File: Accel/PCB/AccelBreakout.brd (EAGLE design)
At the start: 15.2 x 12.7 mm, 10 parts

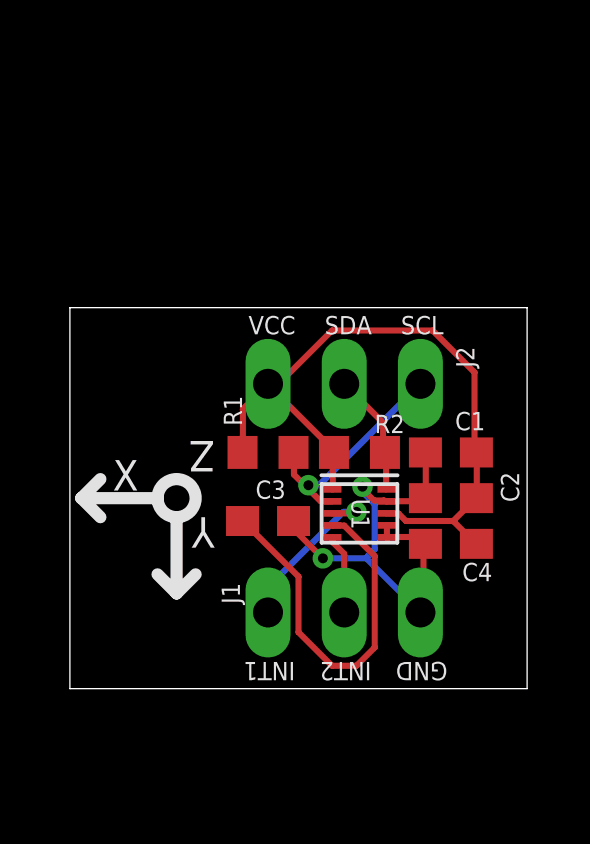
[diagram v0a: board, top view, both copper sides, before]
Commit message: accel - size, layout, labels
Adjusted size to be 0.6" DIP spacing.  Better orientation and position of all
labels.  Completely rerouted to remove all vias.
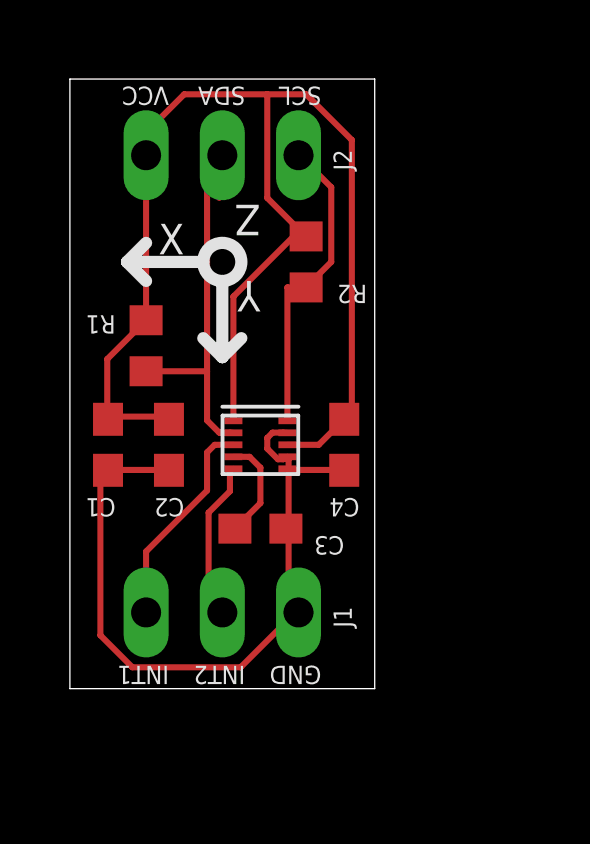
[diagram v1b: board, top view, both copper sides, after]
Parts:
- removed U$23: MMA8653FCR1, ScottSilver:MMA8653FCR1
- added U1: MMA8653FCR1, ScottSilver:MMA8653FCR1
- moved C1 11.4 mm to (1.27, 8.13), turned to 270 degrees
- moved C2 9.56 mm to (3.30, 8.13), turned to 270 degrees
- moved U$3 8.64 mm to (5.08, 17.8)
- moved U$2 8.02 mm to (5.08, 13.6)
- moved R2 6.59 mm to (7.87, 14.2), turned to 90 degrees
- moved R1 5.40 mm to (2.54, 11.4), turned to 90 degrees
- moved C4 4.85 mm to (9.14, 8.13), turned to 270 degrees
- moved U$4 4.06 mm to (5.08, 2.54)
- moved C3 0.36 mm to (6.35, 5.33)
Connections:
- net GND: now also U1.6, U1.7, U1.9; no longer U$23.6, U$23.7, U$23.9
- net INT1: now also U1.3; no longer U$23.3
- net INT2: now also U1.5; no longer U$23.5
- net N$34: now also U1.4; no longer U$23.4
- net SCL: now also U$3.P$2, U1.2; no longer U$23.2, U$3.P$3
- net SDA: now also U$3.P$3, U1.10; no longer U$23.10, U$3.P$2
- net VCC: now also U1.1, U1.8; no longer U$23.1, U$23.8
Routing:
- net VCC: track 24.1 -> 44.9 mm
- net N$34: track 12.6 -> 3.43 mm
- net GND: track 16.4 -> 24.9 mm, vias 2 -> 0
- net SDA: track 4.11 -> 10.3 mm
- net SCL: track 7.63 -> 13.7 mm, vias 1 -> 0
- net INT2: track 2.66 -> 5.35 mm
- net INT1: track 5.65 -> 7.16 mm, vias 1 -> 0
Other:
- board size 15.2 x 12.7 mm -> 10.2 x 20.3 mm
- board text removed: "U1"

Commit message: accel - adjusted direction symbol, replaced parts
Some old parts were missing from raspberrystem.lbr.
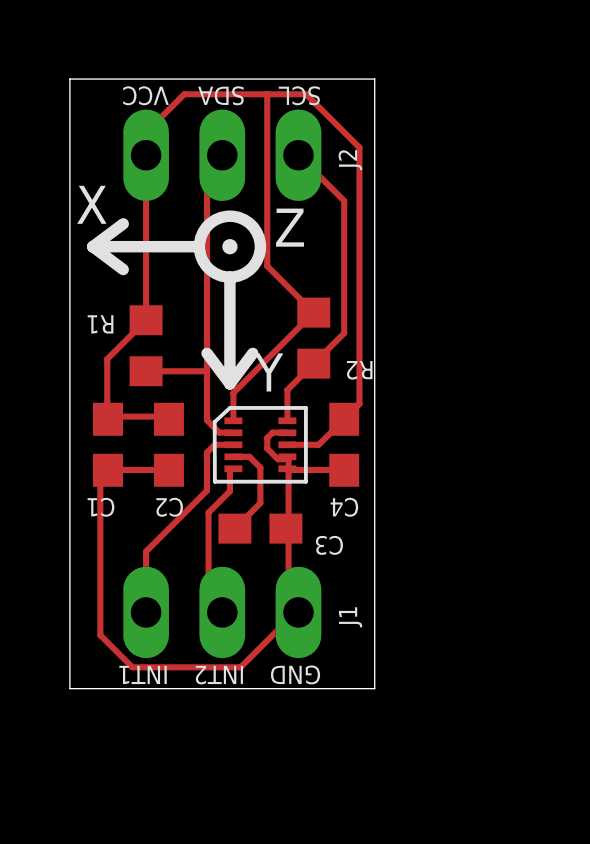
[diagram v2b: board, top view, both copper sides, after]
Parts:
- removed U$2: ACCELDIR, ScottSilver:ACCELDIR
- removed U$3, U$4: DIP1X3MALE, OldScottSilver:DIP1X3MALE
- added J1, J2: (no value), raspberrystem:1X03
- added U$1: (no value), raspberrystem:ACCEL_DIR
- U1: device ScottSilver:MMA8653FCR1 -> raspberrystem:MMA8653FCR1
- moved R2 2.55 mm to (8.13, 11.7)
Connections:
- net GND: now also J1.3; no longer U$4.P$3
- net INT1: now also J1.1; no longer U$4.P$1
- net INT2: now also J1.2; no longer U$4.P$2
- net SCL: now also J2.2; no longer U$3.P$2
- net SDA: now also J2.3; no longer U$3.P$3
- net VCC: now also J2.1; no longer U$3.P$1
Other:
- board text removed: "J1"
- board text removed: "J2"
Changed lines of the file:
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@@
 <text x="3.302" y="0.762" size="0.6096" layer="21" font="vector" rot="SR180">INT1</text>
 <text x="5.842" y="0.762" size="0.6096" layer="21" font="vector" rot="SR180">INT2</text>
-<text x="9.398" y="2.032" size="0.6096" layer="21" font="vector" rot="R90">J1</text>
-<text x="9.398" y="17.272" size="0.6096" layer="21" font="vector" rot="R90">J2</text>
 </plain>
 <attributes>
@@
 </autorouter>
 <elements>
-<element name="U1" library="ScottSilver" package="MMA8653FCR1" value="MMA8653FCR1" x="6.35" y="8.128"/>
+<element name="U1" library="raspberrystem" package="MMA8653FCR1" value="MMA8653FCR1" x="6.35" y="8.128"/>
 <element name="C1" library="resistor" package="C0603" value="0.1uF" x="1.27" y="8.128" smashed="yes" rot="R270">
 <attribute name="NAME" x="1.524" y="6.35" size="0.6096" layer="25" font="vector" rot="SR180"/>
@@
 <attribute name="NAME" x="1.524" y="12.446" size="0.6096" layer="25" font="vector" rot="SR180"/>
 </element>
-<element name="R2" library="resistor" package="R0603" value="10K" x="7.874" y="14.224" smashed="yes" rot="R90">
-<attribute name="NAME" x="9.906" y="13.462" size="0.6096" layer="25" font="vector" rot="SR180"/>
-</element>
-<element name="U$2" library="ScottSilver" package="ACCELDIR" value="ACCELDIR" x="5.08" y="13.589"/>
-<element name="U$3" library="OldScottSilver" package="DIP1X3MALE" value="DIP1X3MALE" x="5.08" y="17.78"/>
-<element name="U$4" library="OldScottSilver" package="DIP1X3MALE" value="DIP1X3MALE" x="5.08" y="2.54"/>
+<element name="R2" library="resistor" package="R0603" value="10K" x="8.128" y="11.684" smashed="yes" rot="R90">
+<attribute name="NAME" x="10.16" y="10.922" size="0.6096" layer="25" font="vector" rot="SR180"/>
+</element>
+<element name="J2" library="raspberrystem" package="1X03" value="" x="5.08" y="17.78" smashed="yes">
+<attribute name="NAME" x="9.5758" y="17.3228" size="0.6096" layer="25" font="vector" ratio="10" rot="R90"/>
+<attribute name="VALUE" x="1.27" y="14.605" size="1.27" layer="27"/>
+</element>
+<element name="J1" library="raspberrystem" package="1X03" value="" x="5.08" y="2.54" smashed="yes">
+<attribute name="NAME" x="9.5758" y="2.0828" size="0.6096" layer="25" font="vector" ratio="10" rot="R90"/>
+<attribute name="VALUE" x="1.27" y="-0.635" size="1.27" layer="27"/>
+</element>
+<element name="U$1" library="raspberrystem" package="ACCEL_DIR" value="" x="5.334" y="14.732" rot="SR180"/>
 </elements>
 <signals>
@@
 <contactref element="R1" pad="2"/>
 <contactref element="R2" pad="2"/>
-<contactref element="U$3" pad="P$1"/>
-<wire x1="9.144" y1="8.978" x2="9.398" y2="8.978" width="0.2032" layer="1"/>
-<wire x1="9.398" y1="8.978" x2="9.398" y2="18.288" width="0.2032" layer="1"/>
-<wire x1="9.398" y1="18.288" x2="7.874" y2="19.812" width="0.2032" layer="1"/>
+<contactref element="J2" pad="1"/>
 <wire x1="7.874" y1="19.812" x2="6.5786" y2="19.812" width="0.2032" layer="1"/>
 <wire x1="6.5786" y1="19.812" x2="3.81" y2="19.812" width="0.2032" layer="1"/>
@@
 <wire x1="1.4224" y1="9.0678" x2="1.27" y2="8.978" width="0.2032" layer="1"/>
 <wire x1="3.2004" y1="9.0678" x2="3.302" y2="8.978" width="0.2032" layer="1"/>
-<wire x1="6.5786" y1="16.3576" x2="7.8232" y2="15.113" width="0.2032" layer="1"/>
-<wire x1="6.5786" y1="19.812" x2="6.5786" y2="16.3576" width="0.2032" layer="1"/>
-<wire x1="7.8232" y1="15.113" x2="7.874" y2="15.074" width="0.2032" layer="1"/>
+<wire x1="6.5786" y1="19.812" x2="6.5786" y2="14.0834" width="0.2032" layer="1"/>
 <wire x1="1.2446" y1="9.0678" x2="1.27" y2="8.978" width="0.2032" layer="1"/>
-<wire x1="5.45" y1="8.928" x2="5.45" y2="13.07" width="0.2032" layer="1"/>
-<wire x1="5.45" y1="13.07" x2="7.62" y2="15.24" width="0.2032" layer="1"/>
-<wire x1="7.62" y1="15.24" x2="7.708" y2="15.24" width="0.2032" layer="1"/>
-<wire x1="7.708" y1="15.24" x2="7.874" y2="15.074" width="0.2032" layer="1"/>
 <wire x1="7.25" y1="8.128" x2="8.294" y2="8.128" width="0.2032" layer="1"/>
 <wire x1="8.294" y1="8.128" x2="9.144" y2="8.978" width="0.2032" layer="1"/>
@@
 <wire x1="2.4892" y1="17.78" x2="2.54" y2="17.78" width="0.2032" layer="1"/>
 <wire x1="2.54" y1="17.78" x2="2.54" y2="12.28" width="0.2032" layer="1"/>
+<wire x1="8.128" y1="12.534" x2="6.5786" y2="14.0834" width="0.2032" layer="1"/>
+<wire x1="5.45" y1="8.928" x2="5.45" y2="9.856" width="0.2032" layer="1"/>
+<wire x1="5.45" y1="9.856" x2="8.128" y2="12.534" width="0.2032" layer="1"/>
+<wire x1="9.144" y1="8.978" x2="9.652" y2="9.486" width="0.2032" layer="1"/>
+<wire x1="9.652" y1="9.486" x2="9.652" y2="18.034" width="0.2032" layer="1"/>
+<wire x1="9.652" y1="18.034" x2="7.874" y2="19.812" width="0.2032" layer="1"/>
 </signal>
 <signal name="GND">
@@
 <contactref element="C4" pad="2"/>
 <contactref element="U1" pad="9"/>
-<contactref element="U$4" pad="P$3"/>
+<contactref element="J1" pad="3"/>
 <wire x1="7.2898" y1="7.6454" x2="7.2898" y2="7.2898" width="0.2032" layer="1"/>
 <wire x1="7.2898" y1="7.6454" x2="7.25" y2="7.728" width="0.2032" layer="1"/>
@@
 <contactref element="U1" pad="10"/>
 <contactref element="R2" pad="1"/>
-<contactref element="U$3" pad="P$3"/>
-<wire x1="8.7122" y1="14.224" x2="8.001" y2="13.5128" width="0.2032" layer="1"/>
-<wire x1="8.7122" y1="16.7132" x2="8.7122" y2="14.224" width="0.2032" layer="1"/>
-<wire x1="7.6454" y1="17.78" x2="8.7122" y2="16.7132" width="0.2032" layer="1"/>
-<wire x1="8.001" y1="13.5128" x2="7.874" y2="13.374" width="0.2032" layer="1"/>
+<contactref element="J2" pad="3"/>
 <wire x1="7.6454" y1="17.78" x2="7.62" y2="17.78" width="0.2032" layer="1"/>
-<wire x1="7.874" y1="13.374" x2="7.25" y2="13.374" width="0.2032" layer="1"/>
-<wire x1="7.25" y1="13.374" x2="7.25" y2="8.928" width="0.2032" layer="1"/>
+<wire x1="7.25" y1="8.928" x2="7.25" y2="9.956" width="0.2032" layer="1"/>
+<wire x1="7.25" y1="9.956" x2="8.128" y2="10.834" width="0.2032" layer="1"/>
+<wire x1="8.128" y1="10.834" x2="9.144" y2="11.85" width="0.2032" layer="1"/>
+<wire x1="7.62" y1="17.78" x2="9.144" y2="16.256" width="0.2032" layer="1"/>
+<wire x1="9.144" y1="16.256" x2="9.144" y2="11.85" width="0.2032" layer="1"/>
 </signal>
 <signal name="SCL">
 <contactref element="U1" pad="2"/>
 <contactref element="R1" pad="1"/>
-<contactref element="U$3" pad="P$2"/>
+<contactref element="J2" pad="2"/>
 <wire x1="4.9784" y1="8.5344" x2="5.334" y2="8.5344" width="0.2032" layer="1"/>
 <wire x1="5.334" y1="8.5344" x2="5.45" y2="8.528" width="0.2032" layer="1"/>
@@
 <signal name="INT1">
 <contactref element="U1" pad="3"/>
-<contactref element="U$4" pad="P$1"/>
+<contactref element="J1" pad="1"/>
 <wire x1="5.45" y1="8.128" x2="4.826" y2="8.128" width="0.2032" layer="1"/>
 <wire x1="4.826" y1="8.128" x2="4.572" y2="7.874" width="0.2032" layer="1"/>
@@
 <signal name="INT2">
 <contactref element="U1" pad="5"/>
-<contactref element="U$4" pad="P$2"/>
+<contactref element="J1" pad="2"/>
 <wire x1="5.334" y1="6.5786" x2="5.334" y2="7.2898" width="0.2032" layer="1"/>
 <wire x1="4.6228" y1="5.8674" x2="5.334" y2="6.5786" width="0.2032" layer="1"/>

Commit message: accel - Resized board and swapped orientation label to bottom
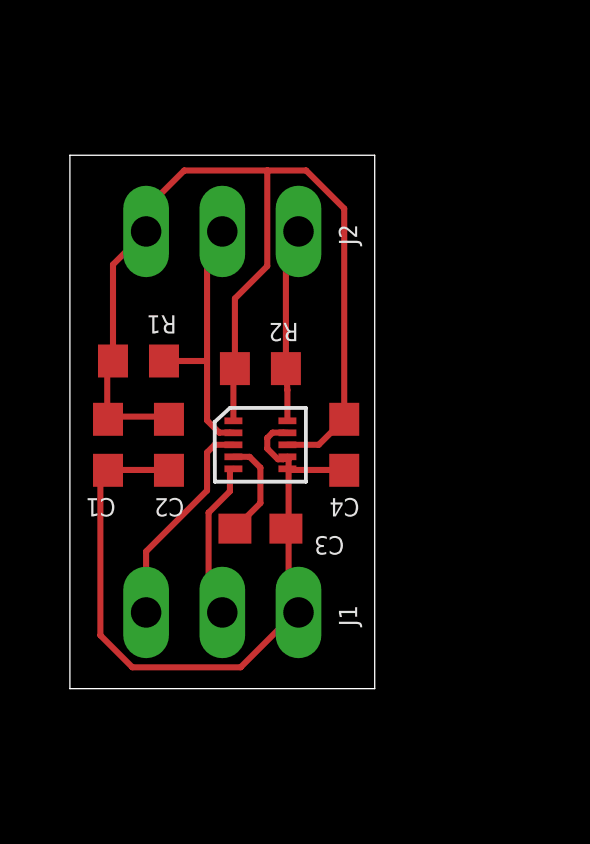
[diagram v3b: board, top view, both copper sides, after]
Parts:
- removed U$1: (no value), raspberrystem:ACCEL_DIR
- added U$2: (no value), raspberrystem:ACCEL_DIR
- moved J2 2.54 mm to (5.08, 15.2)
- moved R2 2.05 mm to (6.35, 10.7), turned to 180 degrees
- moved R1 0.57 mm to (2.29, 10.9), turned to 180 degrees
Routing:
- net VCC: track 44.8 -> 35.6 mm
- net SCL: track 13.7 -> 8.99 mm
- net SDA: track 10.3 -> 6.51 mm
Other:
- board size 10.2 x 20.3 mm -> 10.2 x 17.8 mm
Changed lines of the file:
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@@
 <plain>
 <wire x1="10.16" y1="0" x2="0" y2="0" width="0" layer="20"/>
-<wire x1="0" y1="0" x2="0" y2="20.32" width="0" layer="20"/>
-<wire x1="0" y1="20.32" x2="10.16" y2="20.32" width="0" layer="20"/>
-<wire x1="10.16" y1="20.32" x2="10.16" y2="0" width="0" layer="20"/>
-<text x="3.302" y="20.066" size="0.6096" layer="21" font="vector" rot="SR180">VCC</text>
-<text x="8.382" y="0.762" size="0.6096" layer="21" font="vector" rot="SR180">GND</text>
-<text x="5.842" y="20.066" size="0.6096" layer="21" font="vector" rot="SR180">SDA</text>
-<text x="8.382" y="20.066" size="0.6096" layer="21" font="vector" rot="SR180">SCL</text>
-<text x="3.302" y="0.762" size="0.6096" layer="21" font="vector" rot="SR180">INT1</text>
-<text x="5.842" y="0.762" size="0.6096" layer="21" font="vector" rot="SR180">INT2</text>
+<wire x1="0" y1="0" x2="0" y2="17.78" width="0" layer="20"/>
+<wire x1="0" y1="17.78" x2="10.16" y2="17.78" width="0" layer="20"/>
+<wire x1="10.16" y1="17.78" x2="10.16" y2="0" width="0" layer="20"/>
+<text x="3.429" y="17.526" size="0.6096" layer="22" font="vector" rot="SMR180" align="bottom-right">VCC</text>
+<text x="8.509" y="0.762" size="0.6096" layer="22" font="vector" rot="SMR180" align="bottom-right">GND</text>
+<text x="8.509" y="17.526" size="0.6096" layer="22" font="vector" rot="SMR180" align="bottom-right">SDA</text>
+<text x="5.969" y="17.526" size="0.6096" layer="22" font="vector" rot="SMR180" align="bottom-right">SCL</text>
+<text x="3.429" y="0.762" size="0.6096" layer="22" font="vector" rot="SMR180" align="bottom-right">INT1</text>
+<text x="5.969" y="0.762" size="0.6096" layer="22" font="vector" rot="SMR180" align="bottom-right">INT2</text>
 </plain>
 <attributes>
@@
 <attribute name="NAME" x="9.652" y="6.35" size="0.6096" layer="25" font="vector" rot="SR180"/>
 </element>
-<element name="R1" library="resistor" package="R0603" value="10K" x="2.54" y="11.43" smashed="yes" rot="R90">
-<attribute name="NAME" x="1.524" y="12.446" size="0.6096" layer="25" font="vector" rot="SR180"/>
-</element>
-<element name="R2" library="resistor" package="R0603" value="10K" x="8.128" y="11.684" smashed="yes" rot="R90">
-<attribute name="NAME" x="10.16" y="10.922" size="0.6096" layer="25" font="vector" rot="SR180"/>
-</element>
-<element name="J2" library="raspberrystem" package="1X03" value="" x="5.08" y="17.78" smashed="yes">
-<attribute name="NAME" x="9.5758" y="17.3228" size="0.6096" layer="25" font="vector" ratio="10" rot="R90"/>
-<attribute name="VALUE" x="1.27" y="14.605" size="1.27" layer="27"/>
+<element name="R1" library="resistor" package="R0603" value="10K" x="2.286" y="10.922" smashed="yes" rot="R180">
+<attribute name="NAME" x="3.556" y="12.446" size="0.6096" layer="25" font="vector" rot="SR180"/>
+</element>
+<element name="R2" library="resistor" package="R0603" value="10K" x="6.35" y="10.668" smashed="yes" rot="R180">
+<attribute name="NAME" x="7.62" y="12.192" size="0.6096" layer="25" font="vector" rot="SR180"/>
+</element>
+<element name="J2" library="raspberrystem" package="1X03" value="" x="5.08" y="15.24" smashed="yes">
+<attribute name="NAME" x="9.5758" y="14.7828" size="0.6096" layer="25" font="vector" ratio="10" rot="R90"/>
+<attribute name="VALUE" x="1.27" y="12.065" size="1.27" layer="27"/>
 </element>
 <element name="J1" library="raspberrystem" package="1X03" value="" x="5.08" y="2.54" smashed="yes">
@@
 <attribute name="VALUE" x="1.27" y="-0.635" size="1.27" layer="27"/>
 </element>
-<element name="U$1" library="raspberrystem" package="ACCEL_DIR" value="" x="5.334" y="14.732" rot="SR180"/>
+<element name="U$2" library="raspberrystem" package="ACCEL_DIR" value="" x="6.858" y="10.922" rot="SR180"/>
 </elements>
 <signals>
@@
 <contactref element="R2" pad="2"/>
 <contactref element="J2" pad="1"/>
-<wire x1="7.874" y1="19.812" x2="6.5786" y2="19.812" width="0.2032" layer="1"/>
-<wire x1="6.5786" y1="19.812" x2="3.81" y2="19.812" width="0.2032" layer="1"/>
-<wire x1="3.81" y1="19.812" x2="2.794" y2="18.796" width="0.2032" layer="1"/>
-<wire x1="2.794" y1="18.796" x2="2.794" y2="18.034" width="0.2032" layer="1"/>
-<wire x1="2.794" y1="18.034" x2="2.54" y2="17.78" width="0.2032" layer="1"/>
+<wire x1="7.874" y1="17.272" x2="6.5786" y2="17.272" width="0.2032" layer="1"/>
+<wire x1="6.5786" y1="17.272" x2="3.81" y2="17.272" width="0.2032" layer="1"/>
+<wire x1="3.81" y1="17.272" x2="2.794" y2="16.256" width="0.2032" layer="1"/>
+<wire x1="2.794" y1="16.256" x2="2.794" y2="15.494" width="0.2032" layer="1"/>
+<wire x1="2.794" y1="15.494" x2="2.54" y2="15.24" width="0.2032" layer="1"/>
 <wire x1="3.2004" y1="9.0678" x2="1.4224" y2="9.0678" width="0.2032" layer="1"/>
 <wire x1="1.4224" y1="9.0678" x2="1.27" y2="8.978" width="0.2032" layer="1"/>
 <wire x1="3.2004" y1="9.0678" x2="3.302" y2="8.978" width="0.2032" layer="1"/>
-<wire x1="6.5786" y1="19.812" x2="6.5786" y2="14.0834" width="0.2032" layer="1"/>
+<wire x1="6.5786" y1="17.272" x2="6.5786" y2="14.0834" width="0.2032" layer="1"/>
 <wire x1="1.2446" y1="9.0678" x2="1.27" y2="8.978" width="0.2032" layer="1"/>
 <wire x1="7.25" y1="8.128" x2="8.294" y2="8.128" width="0.2032" layer="1"/>
 <wire x1="8.294" y1="8.128" x2="9.144" y2="8.978" width="0.2032" layer="1"/>
 <wire x1="1.2446" y1="9.0678" x2="1.2446" y2="10.9846" width="0.2032" layer="1"/>
-<wire x1="1.2446" y1="10.9846" x2="2.54" y2="12.28" width="0.2032" layer="1"/>
-<wire x1="2.4892" y1="17.78" x2="2.54" y2="17.78" width="0.2032" layer="1"/>
-<wire x1="2.54" y1="17.78" x2="2.54" y2="12.28" width="0.2032" layer="1"/>
-<wire x1="8.128" y1="12.534" x2="6.5786" y2="14.0834" width="0.2032" layer="1"/>
-<wire x1="5.45" y1="8.928" x2="5.45" y2="9.856" width="0.2032" layer="1"/>
-<wire x1="5.45" y1="9.856" x2="8.128" y2="12.534" width="0.2032" layer="1"/>
-<wire x1="9.144" y1="8.978" x2="9.652" y2="9.486" width="0.2032" layer="1"/>
-<wire x1="9.652" y1="9.486" x2="9.652" y2="18.034" width="0.2032" layer="1"/>
-<wire x1="9.652" y1="18.034" x2="7.874" y2="19.812" width="0.2032" layer="1"/>
+<wire x1="1.2446" y1="10.9846" x2="1.436" y2="10.922" width="0.2032" layer="1"/>
+<wire x1="2.4892" y1="15.24" x2="2.54" y2="15.24" width="0.2032" layer="1"/>
+<wire x1="1.436" y1="10.922" x2="1.436" y2="14.136" width="0.2032" layer="1"/>
+<wire x1="1.436" y1="14.136" x2="2.54" y2="15.24" width="0.2032" layer="1"/>
+<wire x1="9.144" y1="8.978" x2="9.144" y2="16.002" width="0.2032" layer="1"/>
+<wire x1="9.144" y1="16.002" x2="7.874" y2="17.272" width="0.2032" layer="1"/>
+<wire x1="5.5" y1="10.668" x2="5.5" y2="13.0048" width="0.2032" layer="1"/>
+<wire x1="5.5" y1="13.0048" x2="6.5786" y2="14.0834" width="0.2032" layer="1"/>
+<wire x1="5.45" y1="8.928" x2="5.45" y2="10.618" width="0.2032" layer="1"/>
+<wire x1="5.45" y1="10.618" x2="5.5" y2="10.668" width="0.2032" layer="1"/>
 </signal>
 <signal name="GND">
@@
 <contactref element="R2" pad="1"/>
 <contactref element="J2" pad="3"/>
-<wire x1="7.6454" y1="17.78" x2="7.62" y2="17.78" width="0.2032" layer="1"/>
+<wire x1="7.6454" y1="15.24" x2="7.62" y2="15.24" width="0.2032" layer="1"/>
 <wire x1="7.25" y1="8.928" x2="7.25" y2="9.956" width="0.2032" layer="1"/>
-<wire x1="7.25" y1="9.956" x2="8.128" y2="10.834" width="0.2032" layer="1"/>
-<wire x1="8.128" y1="10.834" x2="9.144" y2="11.85" width="0.2032" layer="1"/>
-<wire x1="7.62" y1="17.78" x2="9.144" y2="16.256" width="0.2032" layer="1"/>
-<wire x1="9.144" y1="16.256" x2="9.144" y2="11.85" width="0.2032" layer="1"/>
+<wire x1="7.25" y1="9.956" x2="7.2" y2="10.668" width="0.2032" layer="1"/>
+<wire x1="7.2" y1="10.668" x2="7.2" y2="14.82" width="0.2032" layer="1"/>
+<wire x1="7.2" y1="14.82" x2="7.62" y2="15.24" width="0.2032" layer="1"/>
 </signal>
 <signal name="SCL">
@@
 <wire x1="4.9784" y1="8.5344" x2="5.334" y2="8.5344" width="0.2032" layer="1"/>
 <wire x1="5.334" y1="8.5344" x2="5.45" y2="8.528" width="0.2032" layer="1"/>
-<wire x1="4.9784" y1="16.3576" x2="4.9784" y2="17.78" width="0.2032" layer="1"/>
-<wire x1="4.9784" y1="17.78" x2="5.08" y2="17.78" width="0.2032" layer="1"/>
 <wire x1="4.9784" y1="8.5344" x2="4.572" y2="8.9408" width="0.2032" layer="1"/>
-<wire x1="4.572" y1="8.9408" x2="4.572" y2="10.58" width="0.2032" layer="1"/>
-<wire x1="4.572" y1="10.58" x2="4.572" y2="17.272" width="0.2032" layer="1"/>
-<wire x1="4.572" y1="17.272" x2="5.08" y2="17.78" width="0.2032" layer="1"/>
-<wire x1="2.54" y1="10.58" x2="4.572" y2="10.58" width="0.2032" layer="1"/>
+<wire x1="4.572" y1="8.9408" x2="4.572" y2="10.922" width="0.2032" layer="1"/>
+<wire x1="4.572" y1="10.922" x2="4.572" y2="14.732" width="0.2032" layer="1"/>
+<wire x1="4.572" y1="14.732" x2="5.08" y2="15.24" width="0.2032" layer="1"/>
+<wire x1="3.136" y1="10.922" x2="4.572" y2="10.922" width="0.2032" layer="1"/>
 </signal>
 <signal name="INT1">
